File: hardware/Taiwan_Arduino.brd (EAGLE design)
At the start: 97.4 x 35.6 mm, 43 parts, among them J1 AVR_SPI_PRG_62X3_LOCK, T2 2N2222, U1 ATMEGA328P_PDIP, U2 SPI_FLASH, Y2 16mhz

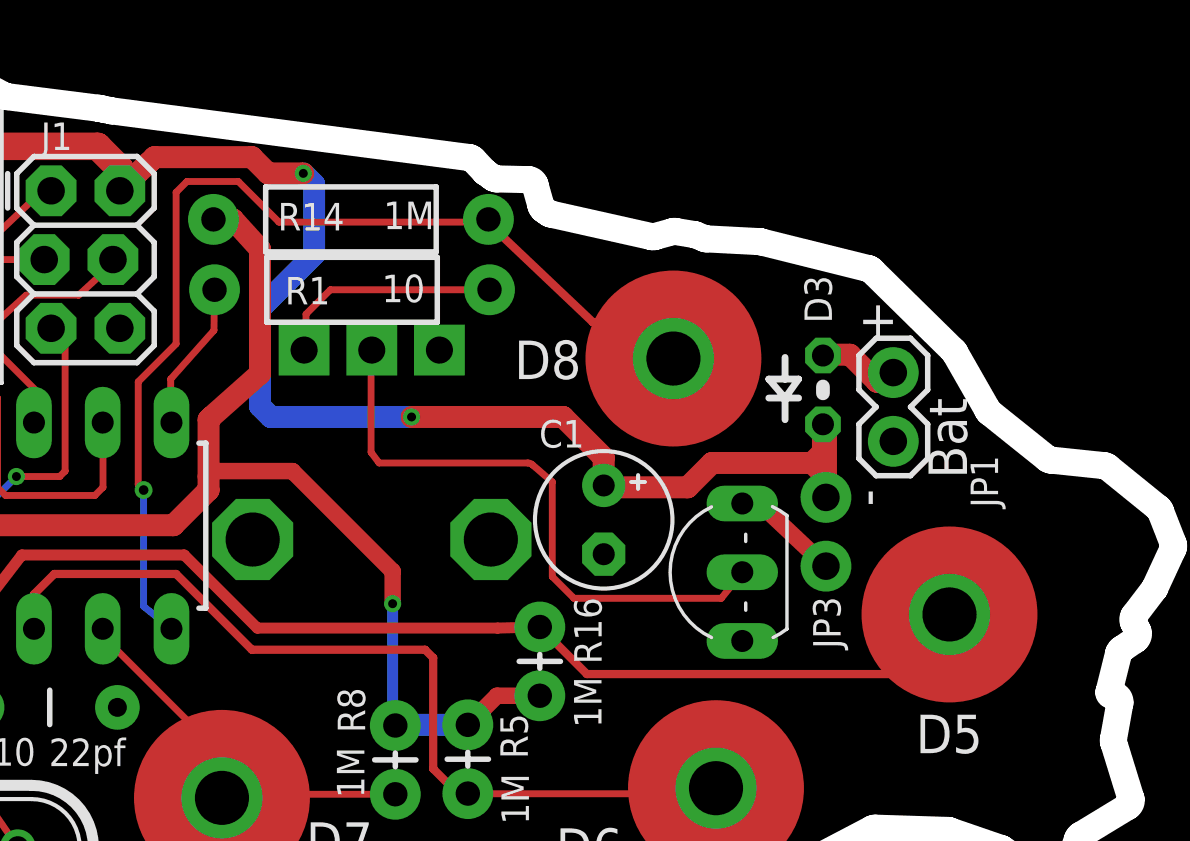
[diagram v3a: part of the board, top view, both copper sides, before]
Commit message: Fix 10 ohm R1
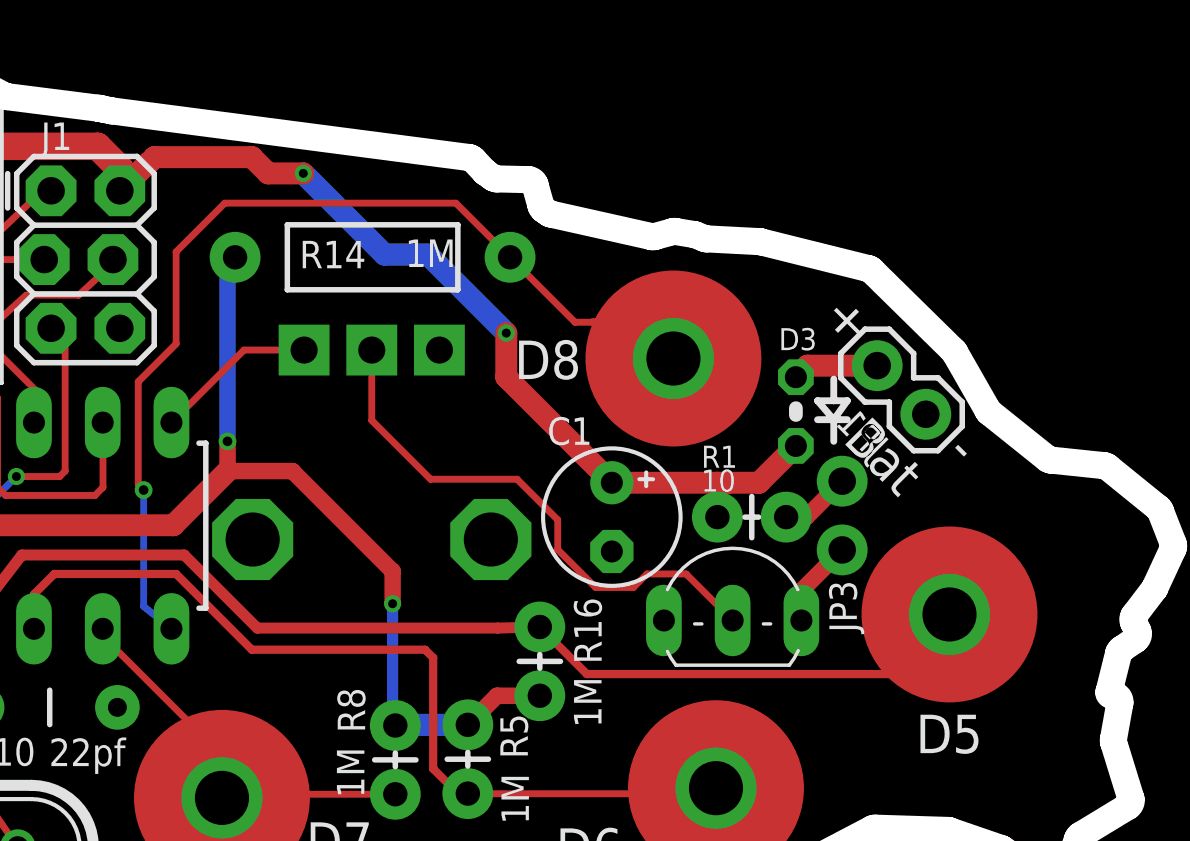
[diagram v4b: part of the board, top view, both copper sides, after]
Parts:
- R1: device SparkFun-Resistors:AXIAL-0.4 -> SparkFun-Resistors:AXIAL-0.1
- moved R1 15.9 mm to (82.0, 21.3), turned to 0 degrees
- moved R14 1.61 mm to (69.3, 30.9)
- moved JP1 1.56 mm to (89.7, 25.1), turned to 135 degrees
- moved D3 1.28 mm to (84.9, 25.2)
- moved T2 1.05 mm to (82.6, 18.8), turned to 0 degrees
- moved JP3 0.85 mm to (86.6, 20.1)
- moved C1 0.32 mm to (78.1, 21.3)
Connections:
- net +5V: now also R1.P$1; no longer JP3.2
- net N$1: now also JP3.2, R1.P$2; no longer R1.P$1, RV1.P$3
- net N$2: now also RV1.P$3; no longer R1.P$2
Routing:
- net +5V: track 158.4 -> 146.7 mm
- net N$1: track 8.51 -> 2.62 mm
- net N$11: track 79.3 -> 75.6 mm, vias 1 -> 2
- net N$22: track 22.3 -> 20.1 mm
- net N$3: track 39.9 -> 37.9 mm
- net N$12: track 4.01 -> 3.23 mm
- net N$18: track 3.71 -> 3.18 mm
